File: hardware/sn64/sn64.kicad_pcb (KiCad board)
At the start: 6 copper layers, 101.8 x 76.5 mm, 421 parts, among them J1 N64_Cartridge_Edge_50, J101 DX07S016JA3R1500, J102 JTAG_SERVICE, J2 SN64_Socket_Joint_2x40, J701 HDMI_A 10029449-111RLF, Q201 2N7002, Q301 BSS138BK, Q302 BSS138BK, Q303 BSS138BK, Q304 BSS138BK, Q305 BSS138BK, Q306 BSS138BK, Q307 BSS138BK, Q308 BSS138BK, U101 USBLC6-2SC6, U102 USBLC6-2SC6, U103 AP2112K-3.3TRG1, U104 FT232HL (rev C), U105 SN74AXC4T774PWR, U106 93AA56BT-I/OT (DNP), U201 SN74LVC4245APWR, U202 SN74LVC4245APWR, U203 SN74LVC4245APWR, U204 SN74LVC4245APWR, U205 SN74LVC4245APWR, U206 SN74LVC4245APWR, U207 SN74LVC4245APWR, U209 SN74LVC244APWR, U210 SN74LVC1G07DBVR, U211 SN74LVC1G07DBVR, U212 SN74LVC1G07DBVR, U213 SN74LVC1G06DBVR, U214 SN74LVC1G06DBVR, U215 SN74LVC1T45DBVR, U216 SN74LVC1T45DBVR, U301 TUSB320IRWBR, U302 TPS259470LRPWR, U303 TPS259470LRPWR, U304 TPS63070RNMR, U305 TLV62569DBVR, U306 TLV62569DBVR, U307 TLV62569DBVR, U308 TPS22918DBVR, U309 TPS259470LRPWR, U310 TPS3700DDCR, U311 TPS3700DDCR, U312 TPS3700DDCR, U313 TPS3700DDCR, U314 TPS3700DDCR, U315 TPS3700DDCR, U316 TPS3808G01DBVR, U317 TMP302ADRLR, U401 LFE5U-85F-6BG381C, U402 SN74CB3Q3384APWR, U403 SN74CB3Q3384APWR, U404 SN74CB3Q3384APWR, U405 W25Q128JVSIQ, U406 SN74LVC1G14DBVR, U407 SN74LVC1G07DBVR, U701 Si5351A-B-GTR, U702 TPD12S016PWR, U703 PCM1808PWR, X701 25MHz CJO05-250003320B30, X702 12.288MHz CJO05-122883320B30, Y101 ABM3B-12.000MHZ-10-1-U-T, Y701 25MHz 10pF

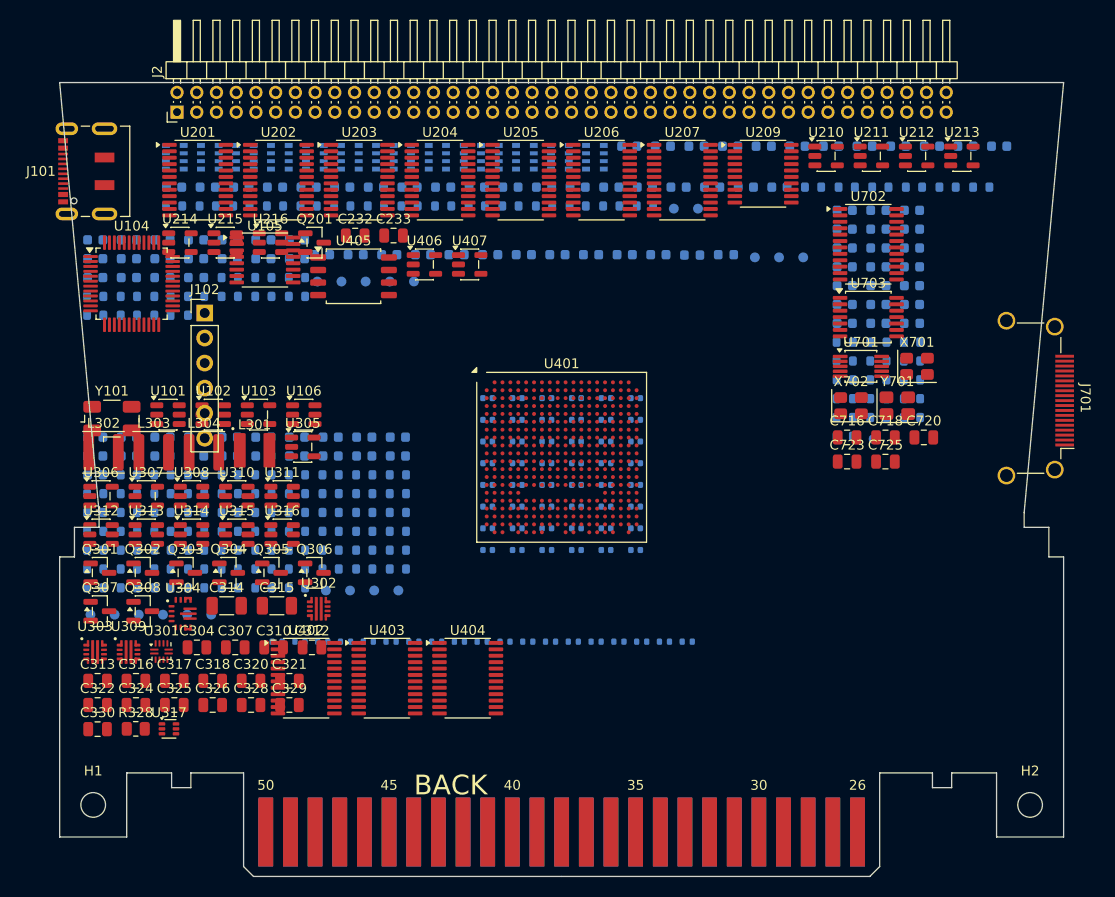
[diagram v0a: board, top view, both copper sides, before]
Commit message: PCB: connectivity-pulled placement with occupancy map, corrected SC64 outline corners, edge keep-outs, rule file
Co-Authored-By: Claude Fable 5.1 <noreply@anthropic.com>
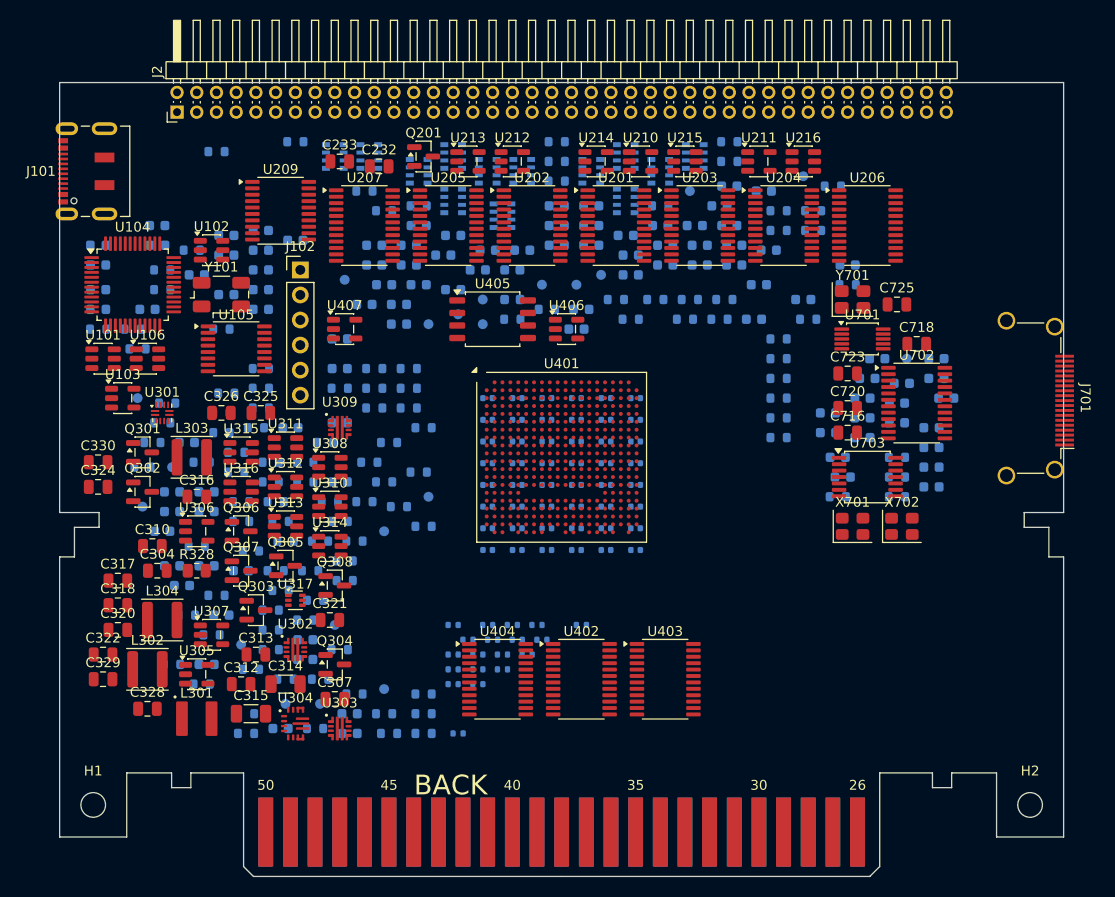
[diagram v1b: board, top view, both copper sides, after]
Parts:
- moved U216 54.6 mm to (24.5, -62.0)
- moved R204 53.8 mm to (-18.0, -57.0)
- moved R207 53.1 mm to (12.5, -46.0)
- moved C213 50.4 mm to (10.5, -51.5)
- moved U213 50.1 mm to (-9.50, -62.0)
- moved U209 49.1 mm to (-28.5, -57.0)
- moved U215 47.3 mm to (12.5, -62.0)
- moved R203 46.9 mm to (-14.5, -57.5)
- moved C211 46.2 mm to (-4.00, -53.0)
- moved C215 46.1 mm to (13.5, -55.5)
- moved U214 43.0 mm to (3.50, -62.0)
- moved U201 42.7 mm to (5.50, -55.5)
- moved U212 41.0 mm to (-5.00, -62.0)
- moved C217 40.1 mm to (14.0, -53.5)
- moved R205 39.6 mm to (-0.50, -60.0)
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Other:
- outline, holes or cut-outs redrawn

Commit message: Decision: SNES video/audio to the console over the cartridge bus is the primary A/V path (design note); six PCB mounting holes
Co-Authored-By: Claude Fable 5.1 <noreply@anthropic.com>
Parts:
- added H3: MountingHole_2.5mm, MountingHole_2.5mm, F.Cu at (-47.5, -16.0)
- added H4: MountingHole_2.5mm, MountingHole_2.5mm, F.Cu at (47.5, -16.0)
- added H5: MountingHole_2.5mm, MountingHole_2.5mm, F.Cu at (-47.5, -66.0)
- added H6: MountingHole_2.5mm, MountingHole_2.5mm, F.Cu at (47.5, -66.0)
- moved U209 68.0 mm to (39.5, -55.0)
- moved Q201 43.0 mm to (29.0, -62.0)
- moved C434 41.7 mm to (24.5, -53.0)
- moved C229 38.2 mm to (-17.5, -55.5)
- moved C230 37.7 mm to (-17.5, -53.5)
- moved R211 37.6 mm to (10.0, -57.5)
- moved R212 37.2 mm to (17.0, -62.5)
- moved C228 35.4 mm to (20.0, -47.5)
- moved R213 34.5 mm to (-0.50, -62.0)
- moved C227 33.7 mm to (20.5, -61.0)
- moved C226 33.0 mm to (21.0, -53.0)
- moved C223 31.4 mm to (-14.0, -54.5)
- moved C222 28.7 mm to (17.5, -51.5)
- moved R320 24.4 mm to (-17.0, -15.0)
- moved C329 24.3 mm to (-33.5, -30.0)
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
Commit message: Remove the on-board HDMI output: the console's own output is the only video path
Owner decision 2026-09-29: the SNES picture and sound reach the TV through the
console (M64 HDMI, N64 AV jack) via the cartridge-bus frame window; the board
has no video output of its own.

FPGA: delete sn64_av_out/av_hdmi_tx/av_serializer, tb_av_out and the vendored
hdl-util/hdmi tree; sn64_clock_init keeps CLK2 powered down (reg 3 = 0xFC) and
writes nothing after start-up; board top keeps one PLL, drops si_clk2/hdmi_*.
Sim suite 38/38; routed 203/208 DP16KD, 113 I/O, 41 % logic, all clocks pass.

Schematic: FPGA sheet rev 0.5-fpga (TMDS/HPD/DDC/si_clk2 pins removed, LPF and
CSV regenerated), A/V sheet draft 0.2-av (J701, TPD12S016, TMDS coupling, R705
gone; Si5351 pin 6 open), root sheet symbols re-packed. ERC 0 errors; all
sheet checks and negative tests pass (FPGA 14/14, A/V 27/27 with new checks).

Board: rebuilt from the new netlist (410 parts, 530 nets), FPGA-support zone
widened; DRC clean apart from the by-design USB-C edge pads and the N64 finger
mask opening. Power budget rows for the HDMI loads removed. Docs updated;
av-output-implementation.md is now the retirement record.

Co-Authored-By: Claude Fable 5.1 <noreply@anthropic.com>
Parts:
- removed C704, C705, C706, C707, C708, C709, C710, C711: 22nF, C_0603_1608Metric
- removed C712, C713, C714: 100nF, C_0603_1608Metric
- removed J701: HDMI_A 10029449-111RLF, HDMI_A_Amphenol_10029449-x01xLF_Horizontal
- removed R705: 0R, R_0603_1608Metric
- removed TP701: CEC_A, TestPoint_Pad_D1.0mm
- removed U702: TPD12S016PWR, TSSOP-24_4.4x7.8mm_P0.65mm
- moved TP406 45.8 mm to (22.0, -44.5)
- moved C434 42.0 mm to (-17.5, -53.0)
- moved C431 39.5 mm to (15.5, -44.0)
- moved C230 38.7 mm to (20.5, -61.0)
- moved C229 38.1 mm to (20.0, -49.0)
- moved C423 36.1 mm to (12.0, -44.0)
- moved C227 35.1 mm to (-14.0, -54.5)
- moved C226 33.0 mm to (-11.5, -47.0)
- moved C422 31.1 mm to (8.50, -44.0)
- moved C421 27.2 mm to (5.00, -44.0)
- moved C453 22.7 mm to (22.5, -52.5)
- moved C450 21.5 mm to (-21.0, -54.0)
- moved C446 21.1 mm to (-21.0, -52.0)
- moved C442 19.8 mm to (19.0, -44.0)
- moved C213 15.1 mm to (-4.50, -53.0)
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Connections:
- U401 pad A12: /hdmi_d2_p -> unconnected-(U401C-PT76A-PadA12)
- U401 pad A13: /hdmi_d2_n -> unconnected-(U401C-PT76B-PadA13)
- U401 pad A14: /hdmi_d1_p -> unconnected-(U401C-PT83A-PadA14)
- U401 pad A16: /hdmi_d0_p -> unconnected-(U401C-PT110A-PadA16)
- U401 pad A17: /hdmi_ck_p -> unconnected-(U401C-PT116A-PadA17)
- U401 pad B16: /hdmi_d0_n -> unconnected-(U401C-PT110B-PadB16)
- U401 pad B18: /hdmi_ck_n -> unconnected-(U401C-PT116B-PadB18)
- U401 pad C14: /hdmi_d1_n -> unconnected-(U401C-PT83B-PadC14)
- U401 pad D15: /hdmi_scl -> unconnected-(U401C-PT107A-PadD15)
- U401 pad E13: /hdmi_hpd -> unconnected-(U401C-PT80B-PadE13)
- U401 pad E15: /hdmi_sda -> unconnected-(U401C-PT107B-PadE15)
- U401 pad F2: /si_clk2 -> unconnected-(U401G-PL44C-PadF2)
- U701 pad 6: /AV clock and cartridge audio/SI_CLK2_SRC -> unconnected-(U701-CLK2-Pad6)

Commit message: PCB: routing preparation (BGA dog-bone fan-out, GND/3V3/1V1 planes, netclasses)
prepare_route.py adds 240 through vias for the used inner balls of the
caBGA-381 (0.4 mm diagonal dog-bones, 0.45/0.2 mm), a GND plane on In1, a
FPGA_3V3 plane on In3 and a FPGA_1V1 island on In4 over the core balls and the
decoupling bands, sets power/usb netclasses in the project file and exports
the Specctra DSN for Freerouting; finish_route.py imports the session and adds
outer GND pours. build_main_pcb.py moves the FPGA decoupling out of the via
field into two bottom-side bands above and below the BGA (the vias landed on
the capacitors before). DRC after preparation: no shorts or clearance errors,
only the by-design USB-C edge pads and the N64 finger mask opening.
Design note: docs/design/pcb-routing.md.

Co-Authored-By: Claude Fable 5.1 <noreply@anthropic.com>
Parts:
- moved TP406 45.6 mm to (-23.5, -47.0)
- moved C450 45.1 mm to (23.0, -44.0)
- moved C442 41.2 mm to (-21.0, -54.0)
- moved C438 39.0 mm to (21.0, -49.0)
- moved C434 38.1 mm to (20.0, -46.0)
- moved C228 35.6 mm to (-14.5, -52.5)
- moved C227 34.5 mm to (20.5, -53.0)
- moved C225 31.5 mm to (-12.5, -50.5)
- moved C423 31.3 mm to (-17.5, -54.5)
- moved C422 27.7 mm to (-18.0, -52.0)
- moved C220 24.7 mm to (-9.00, -50.5)
- moved C421 21.7 mm to (-16.0, -49.5)
- moved C219 21.5 mm to (13.5, -51.5)
- moved C329 16.4 mm to (-37.0, -14.0)
- moved C215 16.2 mm to (-4.00, -51.0)
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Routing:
- net /GND: track 0.00 -> 57.7 mm, vias 0 -> 102
- net /FPGA_1V1: track 0.00 -> 11.3 mm, vias 0 -> 20
- net /FPGA_3V3: track 0.00 -> 10.2 mm, vias 0 -> 18
- net /FPGA/FPGA_VCCAUX: track 0.00 -> 2.26 mm, vias 0 -> 4
- net /si_clk1: track 0.00 -> 0.57 mm, vias 0 -> 1
- net /osc_25: track 0.00 -> 0.57 mm, vias 0 -> 1
- net /cart_pa2: track 0.00 -> 0.57 mm, vias 0 -> 1
- net /cart_address9: track 0.00 -> 0.57 mm, vias 0 -> 1
- net /FPGA/fpga_n64_si_clk: track 0.00 -> 0.57 mm, vias 0 -> 1
- net /FPGA/fpga_n64_reset_n: track 0.00 -> 0.57 mm, vias 0 -> 1
- net /FPGA/fpga_n64_aleh: track 0.00 -> 0.57 mm, vias 0 -> 1
- net /FPGA/fpga_n64_int_n: track 0.00 -> 0.57 mm, vias 0 -> 1
- net /FPGA/fpga_n64_ad9: track 0.00 -> 0.57 mm, vias 0 -> 1
- net /cart_address10: track 0.00 -> 0.57 mm, vias 0 -> 1
- net /cic_data1: track 0.00 -> 0.57 mm, vias 0 -> 1
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- added copper zone on In4.Cu, net /FPGA_1V1
- added copper zone on In3.Cu, net /FPGA_3V3
- added copper zone on In1.Cu, net /GND

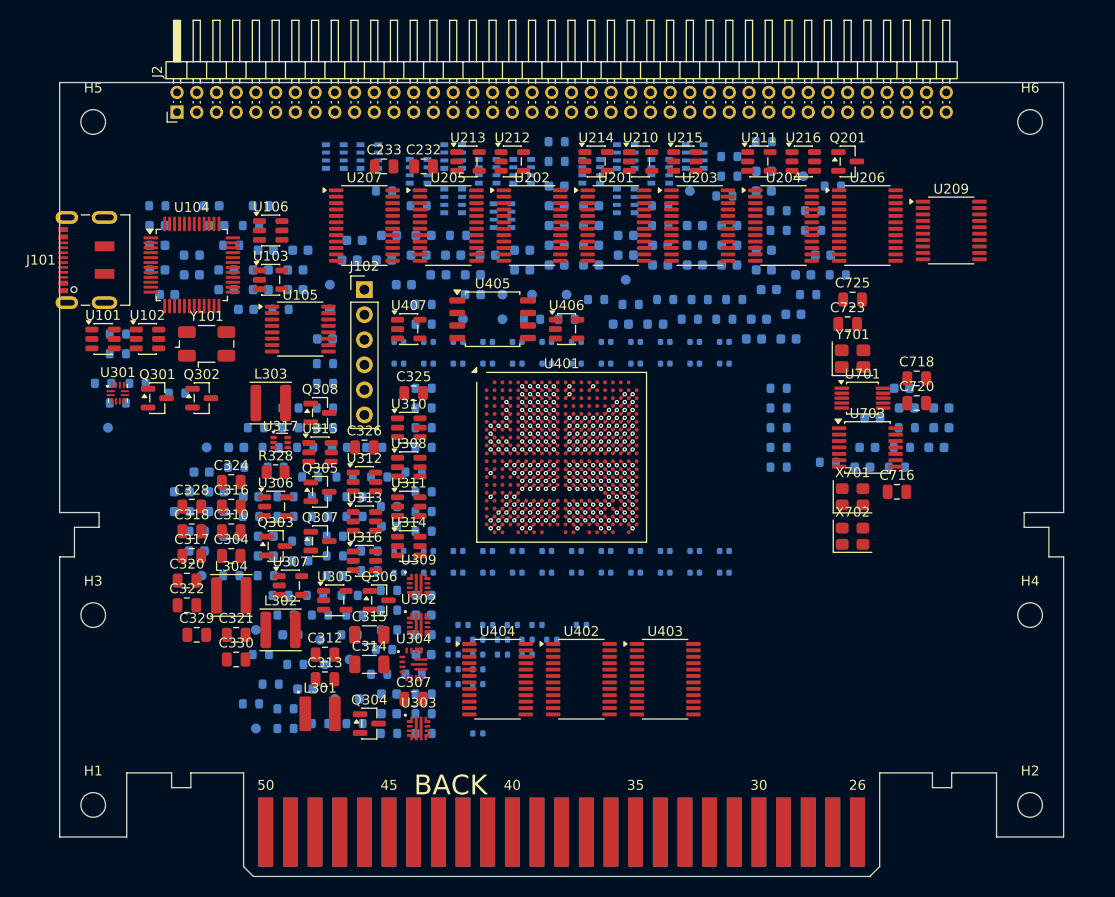
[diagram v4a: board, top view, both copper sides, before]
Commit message: PCB: FPGA rotated 180 degrees so the N64 bank faces the bus switches
The first autoroute run left the N64 bus (fpga_n64_*) unrouted: at 0 degrees
bank 0 faces the top of the board while the bus switches sit at the bottom.
Board rebuilt and re-prepared (fan-out, planes, netclasses); DRC unchanged.

Co-Authored-By: Claude Fable 5.1 <noreply@anthropic.com>
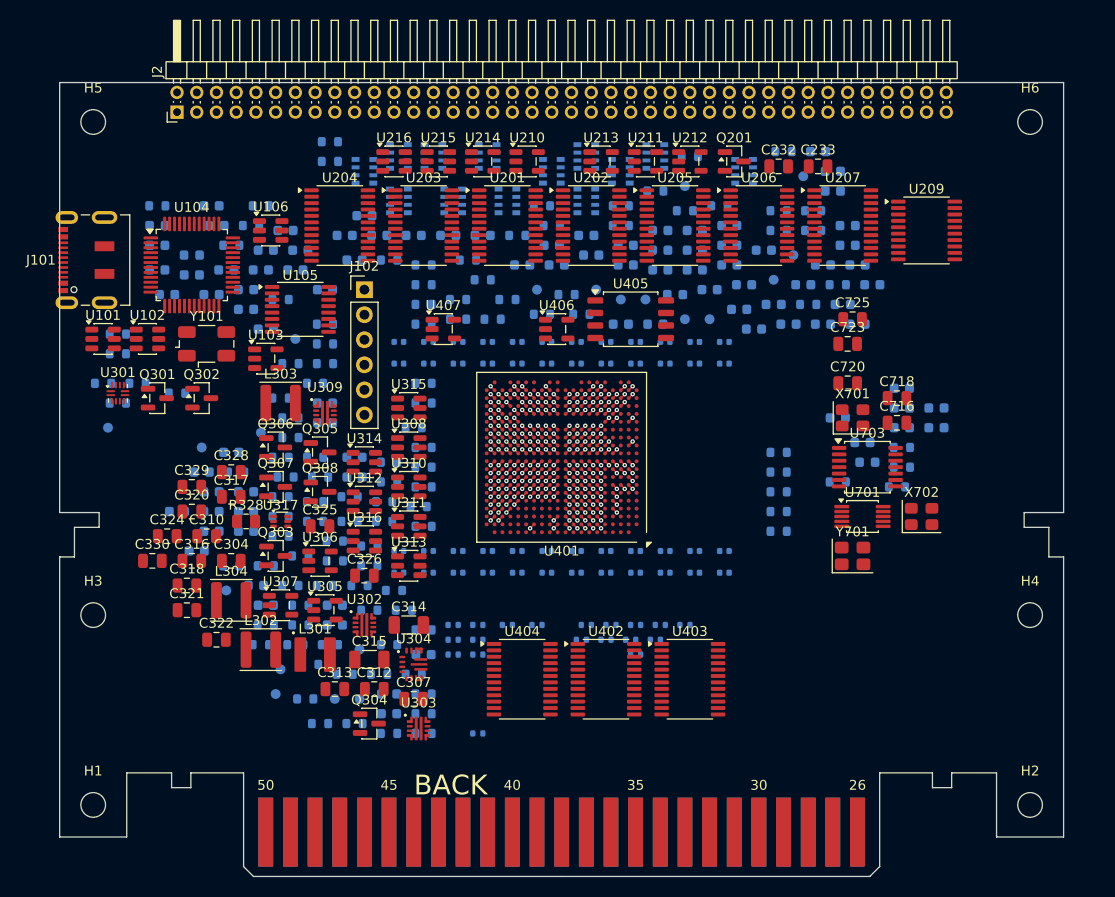
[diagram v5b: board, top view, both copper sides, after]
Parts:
- moved C450 53.0 mm to (-30.0, -45.0)
- moved C446 51.9 mm to (30.0, -45.5)
- moved C442 51.1 mm to (30.0, -51.5)
- moved U207 48.5 mm to (28.5, -55.5)
- moved TP406 47.3 mm to (23.5, -52.5)
- moved TP404 45.0 mm to (21.5, -50.0)
- moved U204 45.0 mm to (-22.5, -55.5)
- moved C233 44.0 mm to (26.0, -61.5)
- moved C229 42.7 mm to (-22.0, -54.5)
- moved C228 42.5 mm to (27.5, -59.0)
- moved C422 41.5 mm to (23.0, -45.5)
- moved U216 41.5 mm to (-17.0, -62.0)
- moved C232 36.0 mm to (22.0, -61.5)
- moved C421 35.8 mm to (19.5, -45.0)
- moved R203 34.1 mm to (22.5, -63.0)
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
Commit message: PCB: plane vias, N64-finger keep-out, PCBWay hole clearance; KiCadRoutingTools fab floors
add_plane_vias.py drops a 0.45/0.2 via next to every GND / FPGA_3V3 / FPGA_1V1
SMD pad on the prepared board (324 placed, 96 left for hand work), checking
pads, tracks, vias, rule areas and the board edge on a 1 mm grid.
prepare_route.py adds a track/via keep-out over the N64 edge tongue on both
outer layers. Hole-to-copper relaxed to 0.2 mm (PCBWay standard 6-layer is
8 mil). fab-pcbway.txt pins KiCadRoutingTools to the board's floors so it no
longer narrows tracks and vias below them. finish_route.py can finish a board
that already carries its routing. KiCad 10 note: PCB_VIA.GetWidth() without a
layer argument asserts and hangs in a hidden dialog; both scripts pass F_Cu.

Co-Authored-By: Claude Fable 5.1 <noreply@anthropic.com>
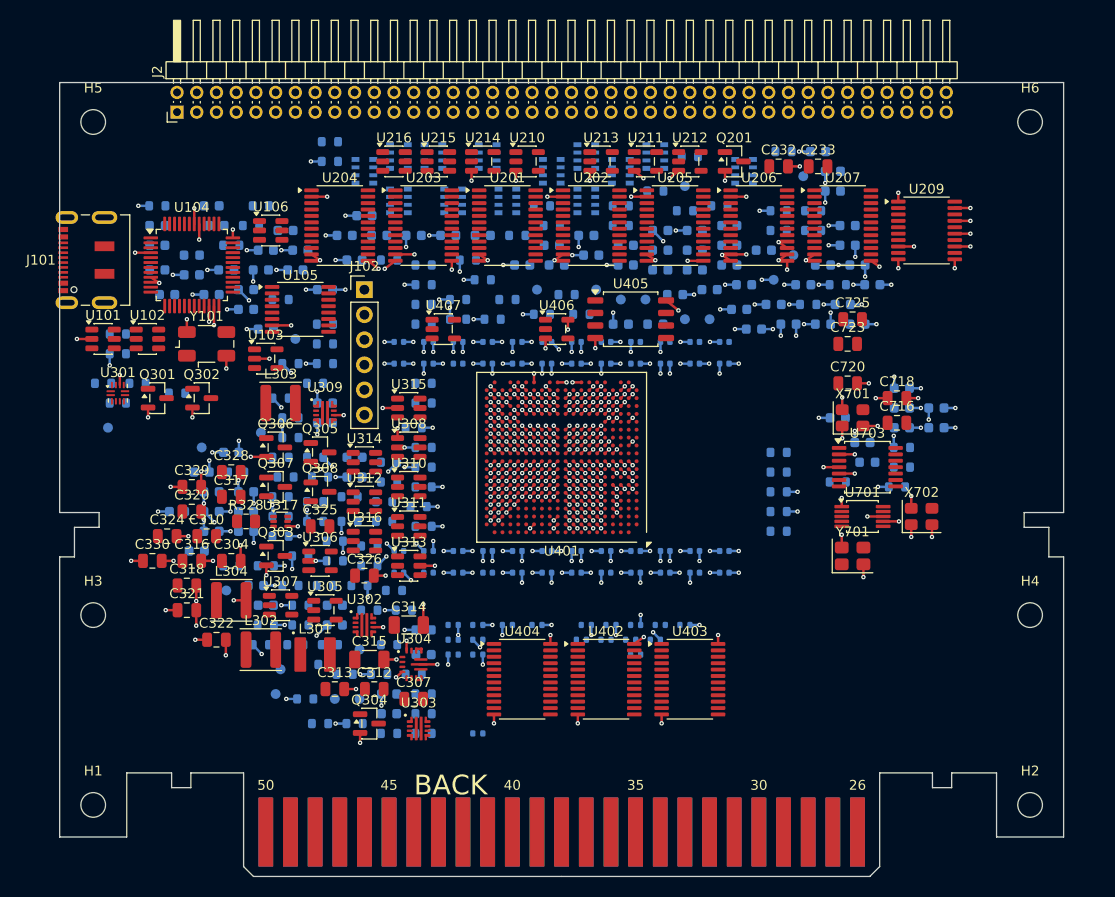
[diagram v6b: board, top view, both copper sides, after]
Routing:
- net /GND: track 57.7 -> 317.0 mm, vias 102 -> 322
- net /FPGA_3V3: track 10.2 -> 96.0 mm, vias 18 -> 95
- net /FPGA_1V1: track 11.3 -> 39.8 mm, vias 20 -> 47
